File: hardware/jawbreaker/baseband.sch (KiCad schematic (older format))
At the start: 109 parts, among them P14 XCVR_CLKOUT, P15 INTR, P16 CLKIN, P17 CLKIN_JMP, P18 OEB, T3 RX_BALUN, T4 TX_BALUN, U17 MAX2837, U18 MAX5864, U19 SI5351C, X1 GSG-XTAL4PIN

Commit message: bom info
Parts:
- removed C105: 22pF, symbol C
- C100, C97, C98: Description (none) -> CAP CER 0.33UF 10V 10% X5R 0402; Manufacturer (none) -> Murata; Part Number (none) -> GRM155R61A334KE15D
- C101, C102, C103, C107, C108, C109, C110, C84, C85, C86, C94, C95, C96, C99: Description (none) -> CAP CER 22PF 50V 5% NP0 0402; Manufacturer (none) -> Murata; Part Number (none) -> GRM1555C1H220JA01D
- C104, C111: Description (none) -> CAP CER 3PF 50V NP0 0402; Manufacturer (none) -> Murata; Part Number (none) -> GRM1555C1H3R0CA01D
- C106: value 1μF -> 1uF; Description (none) -> CAP CER 1UF 10V 20% X5R 0402; Manufacturer (none) -> Murata; Part Number (none) -> GRM155R61A105ME15D
- C114: Description (none) -> CAP CER 3300PF 50V 10% X7R 0402; Manufacturer (none) -> Murata; Part Number (none) -> GRM155R71H332KA01D
- C115, C117: value 1nF -> 10nF; Description (none) -> CAP CER 10000PF 16V 10% X7R 0402; Manufacturer (none) -> Murata; Part Number (none) -> GRM155R71C103KA01D
- C124, C72, C74, C76, C78, C80, C82: value 2.2μF -> 2.2uF; Description (none) -> CAP CER 2.2UF 10V 20% X5R 0402; Manufacturer (none) -> Taiyo Yuden; Part Number (none) -> LMK105BJ225MV-F
- C90: Description (none) -> CAP CER 100PF 50V 5% NP0 0402; Manufacturer (none) -> Murata; Part Number (none) -> GRM1555C1H101JZ01D
- L7: Description (none) -> INDUCTOR HIFREQ 6.2+/-0.3NH 0402; Manufacturer (none) -> Taiyo Yuden; Part Number (none) -> HK10056N2S-T
- P14, P15, R31, R33, R35, R37, R39: Note (none) -> DNP
- R10, R13, R8, R9: Description (none) -> RES 1K OHM 1/16W 5% 0402 SMD; Manufacturer (none) -> Stackpole; Part Number (none) -> RMCF0402JT1K00
- R11, R12, R40, R43, R44, R45: Description (none) -> RES 39 OHM 1/16W 5% 0402 SMD; Manufacturer (none) -> Stackpole; Part Number (none) -> RMCF0402JT39R0
- R20, R21, R22, R23: Description (none) -> RES 0.0 OHM 1/16W 0402 SMD; Manufacturer (none) -> Stackpole; Part Number (none) -> RMCF0402ZT0R00
- R25, R26: Description (none) -> RES TF 1/16W 470 OHM 5% 0402; Manufacturer (none) -> Stackpole; Part Number (none) -> RMCF0402JT470R
- R27, R28: Description (none) -> RES 2K OHM 1/16W 5% 0402 SMD; Manufacturer (none) -> Stackpole; Part Number (none) -> RMCF0402JT2K00
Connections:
- net OVDD is gone; now on net VCC: C123.1, C124.1, R38.2, R39.2, U18.18 (OVDD)
- net VDDOA is gone; now on net VCC: C119.1, R30.2, R31.2, U19.11 (VDDOA)
- net VDDOB is gone; now on net VCC: C120.1, R32.2, R33.2, U19.10 (VDDOB)
- net VDDOC is gone; now on net VCC: C121.1, R34.2, R35.2, U19.18 (VDDOC)
- net VDDOD is gone; now on net VCC: C122.1, R36.2, R37.2, U19.14 (VDDOD)
- net CLK2: now also R44.1; no longer R44.2
- net CLK3: now also R45.1; no longer R45.2
- net CLK4: now also R43.1; no longer R43.2
- net DIN_AD: now also R11.1; no longer R11.2
- net GCK1: now also R44.2; no longer R44.1
- net GCK2: now also R45.2; no longer R45.1
- net LPC_CLK: now also R43.2; no longer R43.1
- net SCLK_AD: now also R12.1; no longer R12.2
- net SSP1_MOSI: now also R11.2; no longer R11.1
- net SSP1_SCK: now also R12.2; no longer R12.1
- net TX_IF: now also T4.1 (S1)

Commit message: misc. corrections
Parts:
- gave numbers to parts that had none: 2
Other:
- note added: "If trace is cut, a jumper should be used\non P17 at all times when an external\nclock is not connected to P16."
- note added: "Install R18 and R19 only\nif 1V8 is used for U18."
- note added: "Install only if 1.8 V output\nis desired and VDDOA\nis set to VCC."
- note removed: "If trace is cut, a jumper should be used\non P9 at all times when an external\nclock is not connected to P8."
- note removed: "Install R37 only if 1.8 V\noutput is desired and VDDOA\nis set to VCC."
- note removed: "Install R40 and R41 only\nif 1V8 is used for U1."
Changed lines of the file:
@@
-EESchema Schematic File Version 2  date Thu Aug 30 11:17:10 2012
+EESchema Schematic File Version 2  date Sun Sep  2 14:58:26 2012
 LIBS:power
 LIBS:device
@@
 Sheet 3 4
 Title "jawbreaker baseband"
-Date "30 aug 2012"
+Date "2 sep 2012"
 Rev ""
 Comp "Copyright 2012 Michael Ossmann"
@@
 FIXME: optional VCC filtering or LDO
 $Comp
-L C C?
+L C C105
 U 1 1 503F888A
 P 3900 2700
-F 0 "C?" H 3950 2800 50  0000 L CNN
+F 0 "C105" H 3950 2800 50  0000 L CNN
 F 1 "10uF" H 3950 2600 50  0000 L CNN
 F 4 "Murata" H 3900 2700 60  0001 C CNN "Manufacturer"
@@
 $EndComp
 $Comp
-L FILTER FB?
+L FILTER FB2
 U 1 1 503F885C
 P 4300 2300
-F 0 "FB?" H 4300 2450 60  0000 C CNN
+F 0 "FB2" H 4300 2450 60  0000 C CNN
 F 1 "FILTER" H 4300 2200 60  0000 C CNN
 F 4 "Murata" H 4300 2300 60  0001 C CNN "Manufacturer"
@@
 VDDOC
 Text Notes 2950 9500 0    40   ~ 0
-If trace is cut, a jumper should be used\non P9 at all times when an external\nclock is not connected to P8.
+If trace is cut, a jumper should be used\non P17 at all times when an external\nclock is not connected to P16.
 $Comp
 L GND #PWR162
@@
 VDDOA
 Text Notes 1150 3750 0    40   ~ 0
-Install R40 and R41 only\nif 1V8 is used for U1.
+Install R18 and R19 only\nif 1V8 is used for U18.
 Text Label 2700 3400 2    40   ~ 0
 SCLK_AD
@@
 $EndComp
 Text Notes 6300 9200 0    40   ~ 0
-Install R37 only if 1.8 V\noutput is desired and VDDOA\nis set to VCC.
+Install only if 1.8 V output\nis desired and VDDOA\nis set to VCC.
 $Comp
 L GND #PWR166

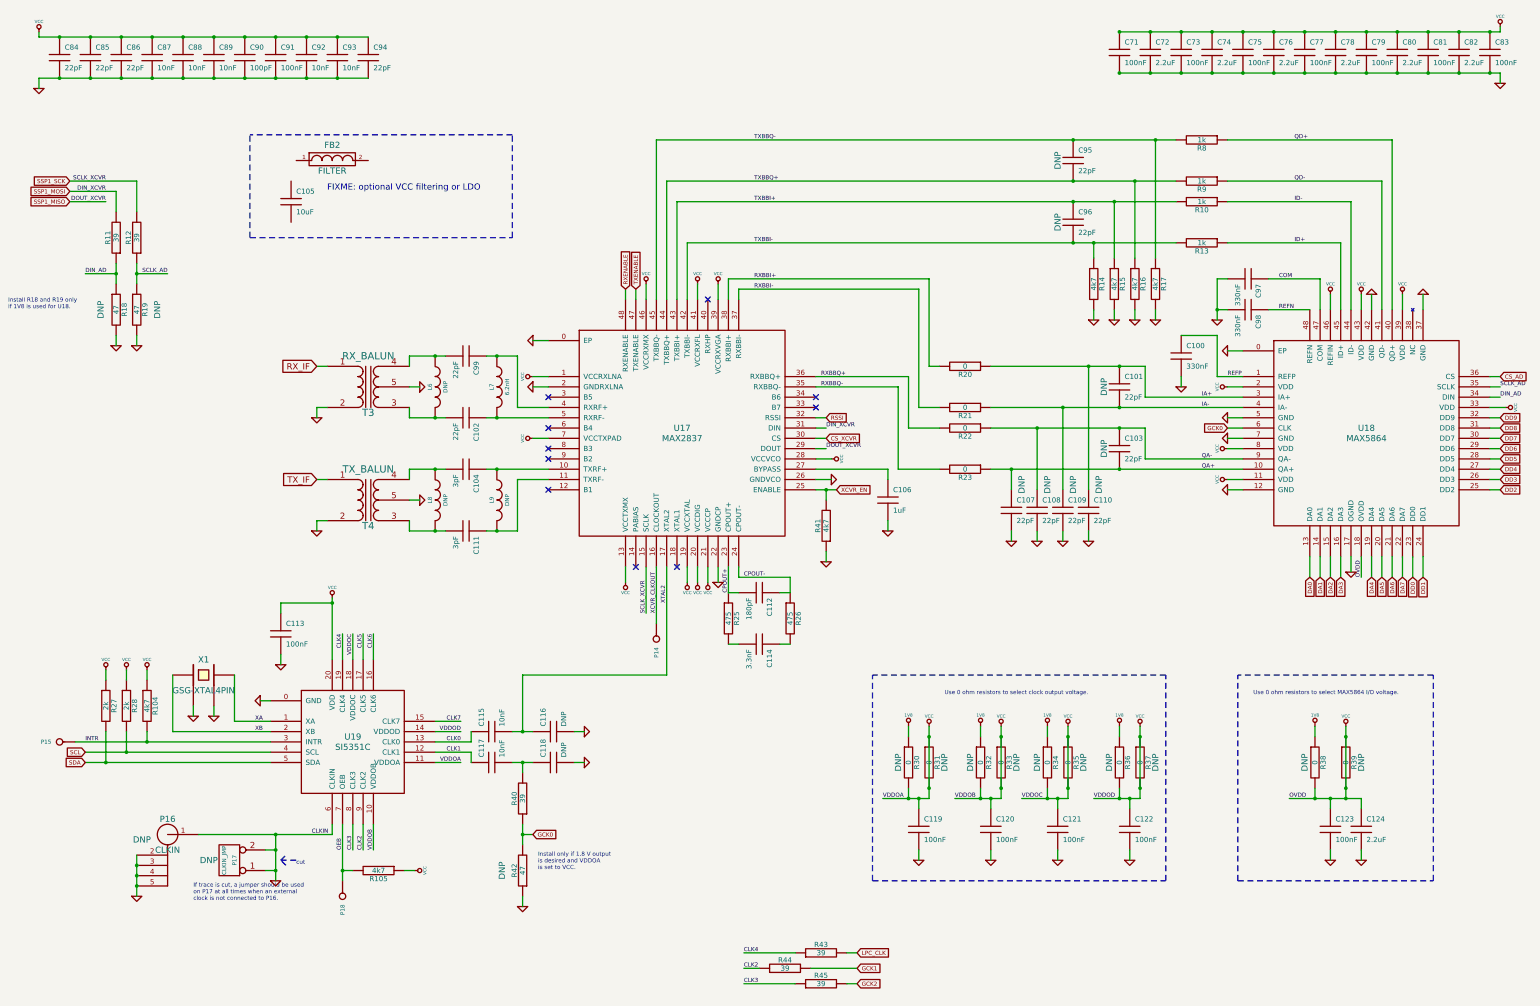
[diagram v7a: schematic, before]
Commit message: optional RF LDO
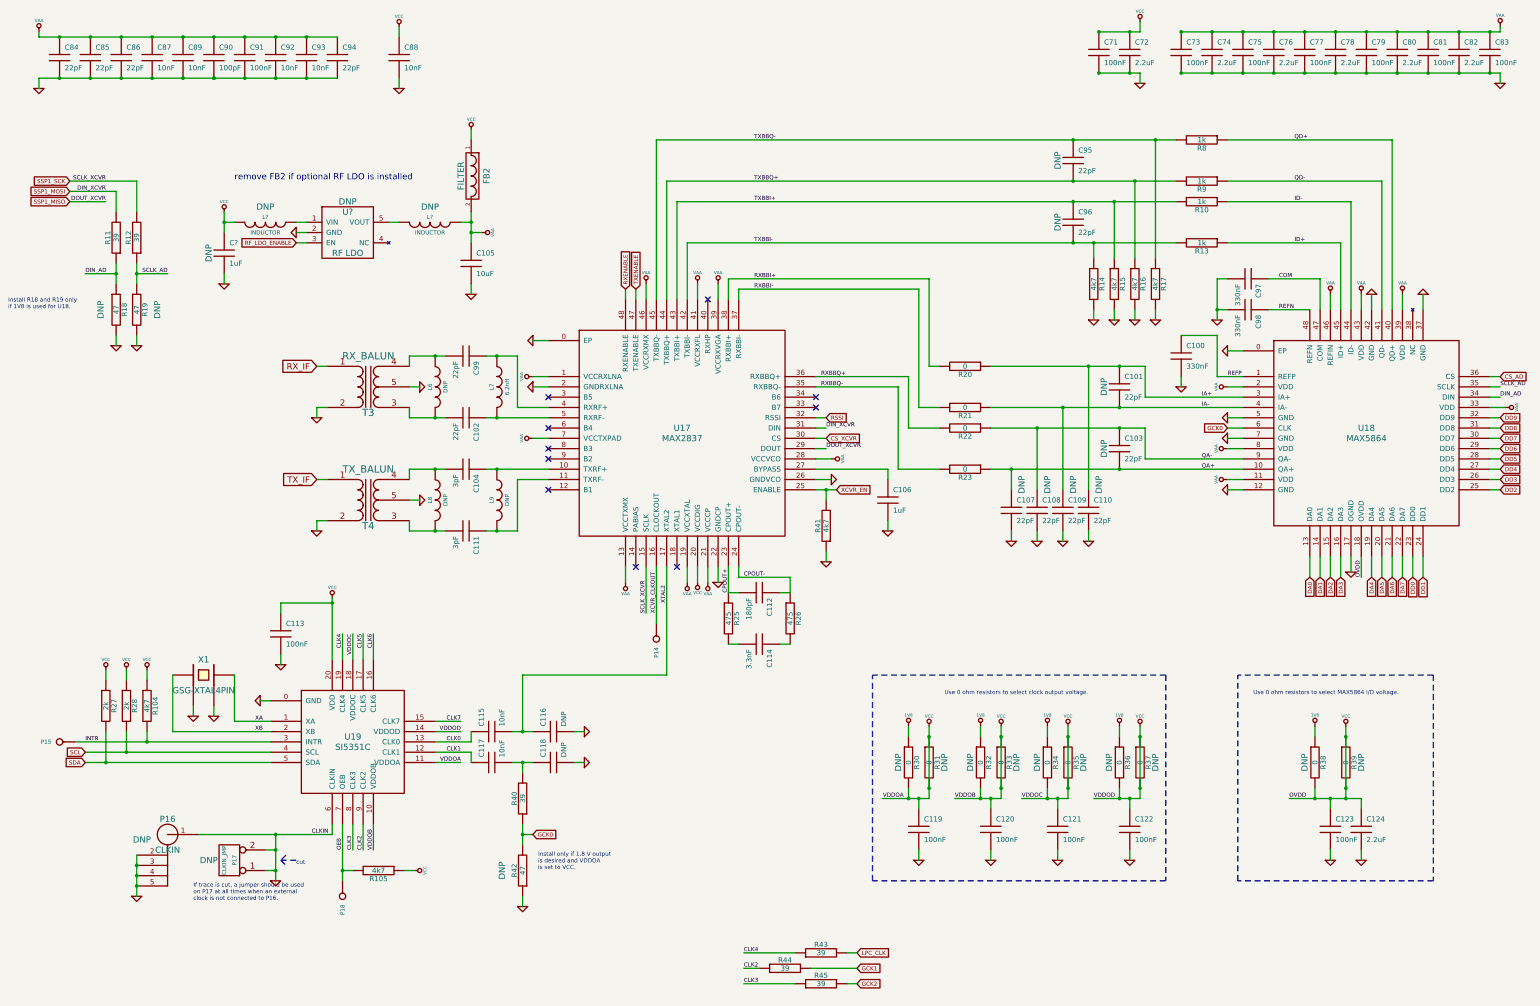
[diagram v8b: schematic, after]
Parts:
- added C?: 1uF, symbol C
- added L? (x2): INDUCTOR, symbol INDUCTOR
- added U?: RF LDO, symbol NCP699
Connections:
- net GND: now also C105.2, C?.2, U?.2 (GND)
- net VCC: now also FB2.1, C?.1, L?.2; no longer C73.1, C74.1, C75.1, C76.1, C77.1, C78.1, C79.1, C80.1, C81.1, C82.1, C83.1, C84.1, C85.1, C86.1, C87.1, C89.1, C90.1, C91.1, C92.1, C93.1, C94.1, U17.1 (VCCRXLNA), U17.13 (VCCTXMX), U17.19 (VCCXTAL), U17.21 (VCCCP), U17.28 (VCCVCO), U17.39 (VCCRXVGA), U17.41 (VCCRXFL), U17.46 (VCCRXMX), U17.7 (VCCTXPAD), U18.11 (VDD), U18.2 (VDD), U18.33 (VDD), U18.39 (VDD), U18.43 (VDD), U18.46 (REFIN), U18.8 (VDD)
- net VAA: now reaches FB2.2
- net VAA: now also C105.1, C73.1, C74.1, C75.1, C76.1, C77.1, C78.1, C79.1, C80.1, C81.1, C82.1, C83.1, C84.1, C85.1, C86.1, C87.1, C89.1, C90.1, C91.1, C92.1, C93.1, C94.1, U17.1 (VCCRXLNA), U17.13 (VCCTXMX), U17.19 (VCCXTAL), U17.21 (VCCCP), U17.28 (VCCVCO), U17.39 (VCCRXVGA), U17.41 (VCCRXFL), U17.46 (VCCRXMX), U17.7 (VCCTXPAD), U18.11 (VDD), U18.2 (VDD), U18.33 (VDD), U18.39 (VDD), U18.43 (VDD), U18.46 (REFIN), U18.8 (VDD), L?.1
- new net: L?.1, U?.1 (VIN)
- new net: L?.2, U?.5 (VOUT)
- new net RF_LDO_ENABLE: U?.3 (EN)
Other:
- note added: "remove FB2 if optional RF LDO is installed"
- note removed: "FIXME: optional VCC filtering or LDO"
- moved on the sheet: C105, C71, C72, C88, C89, C90, C91, C92, C93, C94, FB2
